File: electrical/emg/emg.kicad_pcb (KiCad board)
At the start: 4 copper layers, 70 x 37 mm, 98 parts, among them J1 USB_B, J10 Ref, J11 Conn_01x05, J12 Conn_01x05, J13 Conn_01x05, J14 T3, J15 T3, J16 T3, J17 T3, J2 swd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

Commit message: Done with digital part. More or less...
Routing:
- net /v_ref: track 149.2 -> 228.8 mm
- net VDD: track 98.5 -> 127.8 mm, vias 4 -> 5
- net Net-(C17-Pad2): track 7.55 -> 9.44 mm
- net Net-(C16-Pad1): track 5.22 -> 6.83 mm
- net Net-(C24-Pad2): track 6.21 -> 7.81 mm
- net /vbus: track 29.9 -> 30.7 mm
- net GND: track 244.4 -> 244.9 mm
- added copper zone on B.Cu, net GND
- added copper zone on F.Cu, net GND
- added copper zone on In1.Cu, net GND
- added copper zone on B.Cu, net GNDA
- added copper zone on F.Cu, net GNDA
- added copper zone on In1.Cu, net GNDA
- added copper zone on In2.Cu, net VDD
- added copper zone on In2.Cu, net VDDA

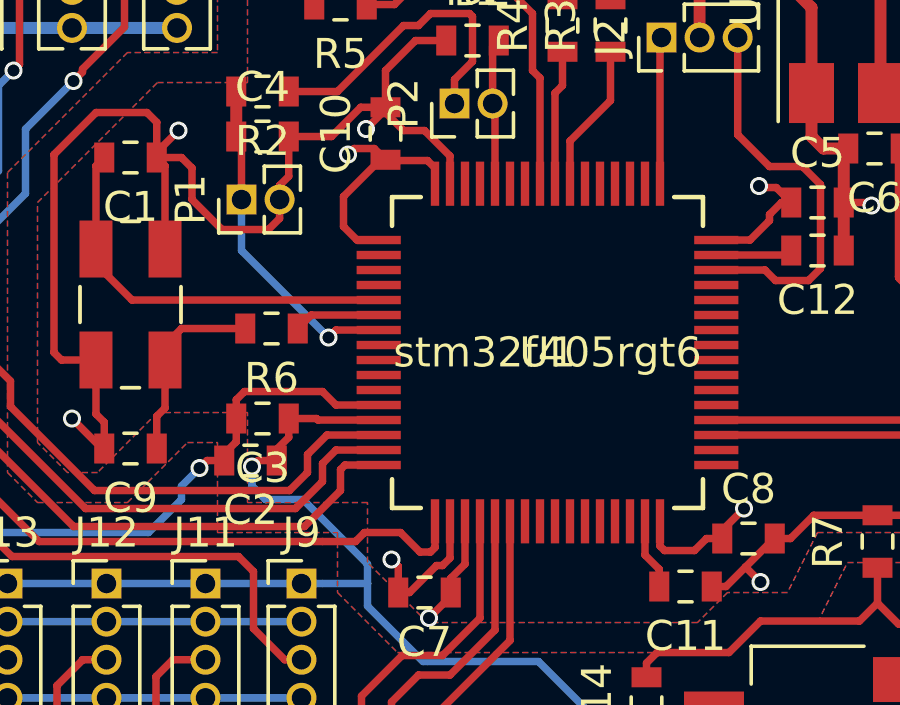
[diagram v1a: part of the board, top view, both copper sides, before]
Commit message: Connected grounds undernear the MCU.
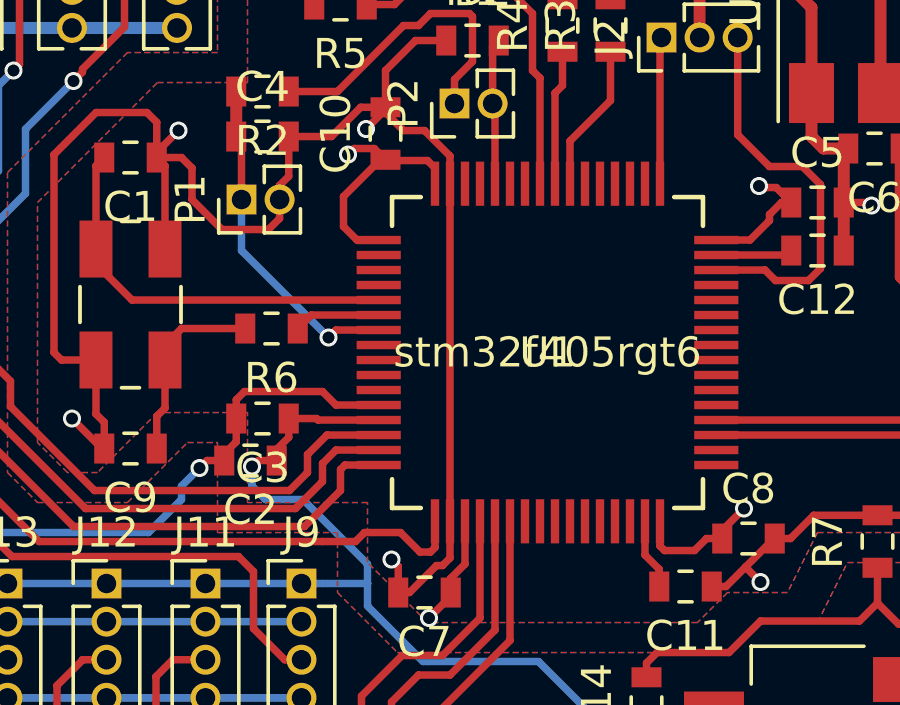
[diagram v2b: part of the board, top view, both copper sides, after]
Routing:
- net GND: track 244.9 -> 256.2 mm
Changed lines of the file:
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@@
     (links 217)
     (no_connects 0)
-    (area 117.924999 81.924999 188.075001 119.075001)
+    (area 103.150001 80.738095 193.525001 130.700001)
     (thickness 1.6)
     (drawings 6)
-    (tracks 945)
+    (tracks 946)
     (zones 0)
     (modules 98)
@@
   (page A4)
   (layers
-    (0 F.Cu signal hide)
+    (0 F.Cu signal)
     (1 In1.Cu signal hide)
-    (2 In2.Cu signal)
+    (2 In2.Cu signal hide)
     (31 B.Cu signal hide)
     (32 B.Adhes user)
@@
   (gr_line (start 188 82) (end 188 119) (angle 90) (layer Edge.Cuts) (width 0.15))
   (gr_line (start 118 82) (end 188 82) (angle 90) (layer Edge.Cuts) (width 0.15))
+  (segment (start 160.749999 95.3739) (end 160.749999 106.6261) (width 0.25) (layer F.Cu) (net 1) (status C00000))
   (segment (start 158.8 107.9) (end 158.8 107.5) (width 0.25) (layer In1.Cu) (net 1))
   (segment (start 159.025 108.125) (end 158.8 107.9) (width 0.25) (layer F.Cu) (net 1))
@@
   (segment (start 158.6 93) (end 158.6 92.825) (width 0.25) (layer F.Cu) (net 1))
   (segment (start 160.749999 106.6261) (end 160.749999 107.850001) (width 0.25) (layer F.Cu) (net 1))
-  (segment (start 159.4 109) (end 159.025 109) (width 0.25) (layer F.Cu) (net 1))
-  (segment (start 160.3 108.1) (end 159.4 109) (width 0.25) (layer F.Cu) (net 1))
-  (segment (start 160.5 108.1) (end 160.3 108.1) (width 0.25) (layer F.Cu) (net 1))
   (segment (start 160.749999 107.850001) (end 160.5 108.1) (width 0.25) (layer F.Cu) (net 1))
+  (segment (start 160.5 108.1) (end 160.3 108.1) (width 0.25) (layer F.Cu) (net 1))
+  (segment (start 160.3 108.1) (end 159.4 109) (width 0.25) (layer F.Cu) (net 1))
+  (segment (start 159.4 109) (end 159.025 109) (width 0.25) (layer F.Cu) (net 1))
   (segment (start 155.07 95.9) (end 155.07 95.43) (width 0.25) (layer F.Cu) (net 1))
   (segment (start 155.07 95.43) (end 155.375 95.125) (width 0.25) (layer F.Cu) (net 1))
